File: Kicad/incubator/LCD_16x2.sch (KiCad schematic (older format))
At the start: 6 parts, among them SW2 Rotary_Encoder_Switch

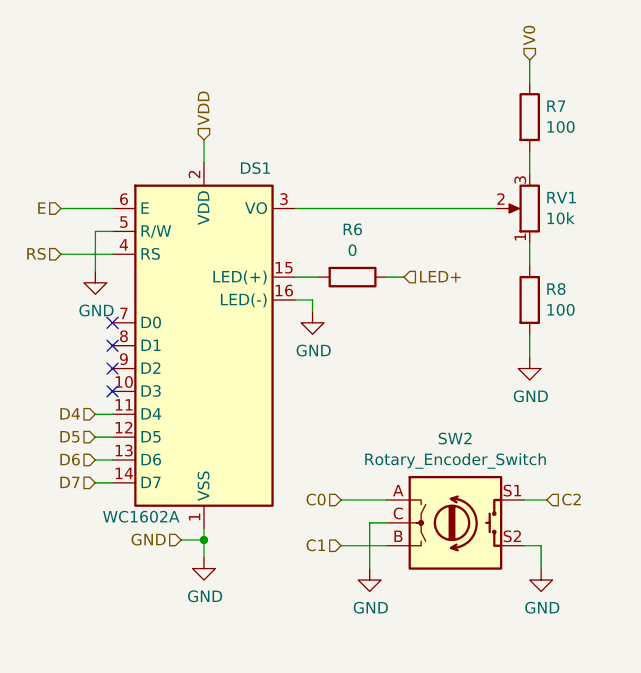
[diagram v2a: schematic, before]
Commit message: fix: iss #1: add ERROR and BLINKING LED, iss #2: solved
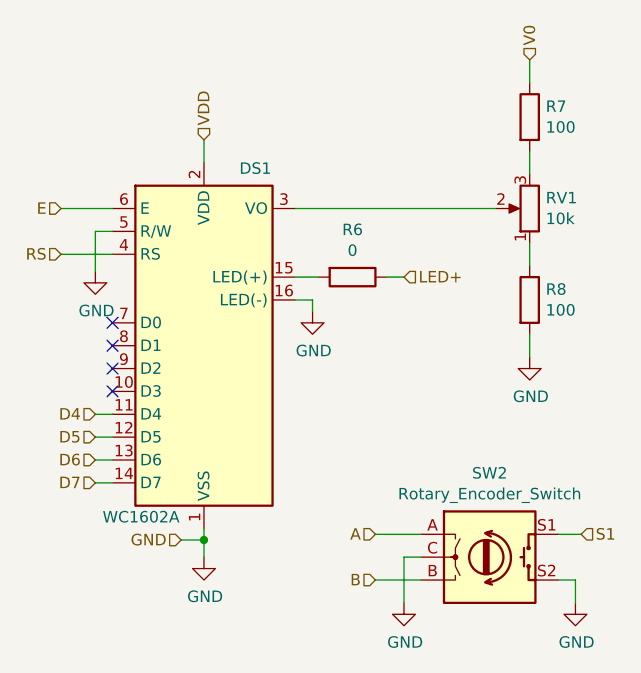
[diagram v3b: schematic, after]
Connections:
- net C0 renamed A
- net C1 renamed B
- net C2 renamed S1
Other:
- moved on the sheet: SW2
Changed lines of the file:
@@
 NoConn ~ 5000 3975
 Wire Wire Line
-	6200 4450 6000 4450
-Wire Wire Line
-	6200 4650 6000 4650
-Wire Wire Line
-	6875 4650 6800 4650
-Wire Wire Line
-	6875 4750 6875 4650
+	6350 4600 6150 4600
+Wire Wire Line
+	6350 4800 6150 4800
+Wire Wire Line
+	7025 4800 6950 4800
+Wire Wire Line
+	7025 4900 7025 4800
 $Comp
 L incubator-rescue:GND-power #PWR?
 U 1 1 611BC109
-P 6875 4750
+P 7025 4900
 AR Path="/611BC109" Ref="#PWR?"  Part="1"
 AR Path="/611AEB1E/611BC109" Ref="#PWR0120"  Part="1"
-F 0 "#PWR0120" H 6875 4500 50  0001 C CNN
-F 1 "GND" H 6880 4577 50  0000 C CNN
-F 2 "" H 6875 4750 50  0001 C CNN
-F 3 "" H 6875 4750 50  0001 C CNN
-	1    6875 4750
-	1    0    0    -1
-$EndComp
-Wire Wire Line
-	6900 4450 6800 4450
-Wire Wire Line
-	6125 4550 6125 4750
-Wire Wire Line
-	6200 4550 6125 4550
+F 0 "#PWR0120" H 7025 4650 50  0001 C CNN
+F 1 "GND" H 7030 4727 50  0000 C CNN
+F 2 "" H 7025 4900 50  0001 C CNN
+F 3 "" H 7025 4900 50  0001 C CNN
+	1    7025 4900
+	1    0    0    -1
+$EndComp
+Wire Wire Line
+	6275 4700 6275 4900
+Wire Wire Line
+	6350 4700 6275 4700
 $Comp
 L incubator-rescue:GND-power #PWR?
 U 1 1 611BC115
-P 6125 4750
+P 6275 4900
 AR Path="/611BC115" Ref="#PWR?"  Part="1"
 AR Path="/611AEB1E/611BC115" Ref="#PWR0121"  Part="1"
-F 0 "#PWR0121" H 6125 4500 50  0001 C CNN
-F 1 "GND" H 6130 4577 50  0000 C CNN
-F 2 "" H 6125 4750 50  0001 C CNN
-F 3 "" H 6125 4750 50  0001 C CNN
-	1    6125 4750
+F 0 "#PWR0121" H 6275 4650 50  0001 C CNN
+F 1 "GND" H 6280 4727 50  0000 C CNN
+F 2 "" H 6275 4900 50  0001 C CNN
+F 3 "" H 6275 4900 50  0001 C CNN
+	1    6275 4900
 	1    0    0    -1
 $EndComp
@@
 L incubator-rescue:Rotary_Encoder_Switch-Device SW?
 U 1 1 611BC160
-P 6500 4550
+P 6650 4700
 AR Path="/611BC160" Ref="SW?"  Part="1"
 AR Path="/611AEB1E/611BC160" Ref="SW2"  Part="1"
-F 0 "SW2" H 6500 4917 50  0000 C CNN
-F 1 "Rotary_Encoder_Switch" H 6500 4826 50  0000 C CNN
-F 2 "Rotary_Encoder:RotaryEncoder_Alps_EC11E-Switch_Vertical_H20mm" H 6350 4710 50  0001 C CNN
-F 3 "~" H 6500 4810 50  0001 C CNN
-	1    6500 4550
+F 0 "SW2" H 6650 5067 50  0000 C CNN
+F 1 "Rotary_Encoder_Switch" H 6650 4976 50  0000 C CNN
+F 2 "Rotary_Encoder:RotaryEncoder_Alps_EC11E-Switch_Vertical_H20mm" H 6500 4860 50  0001 C CNN
+F 3 "~" H 6650 4960 50  0001 C CNN
+	1    6650 4700
 	1    0    0    -1
 $EndComp
@@
 Wire Wire Line
 	5400 4625 5400 4575
-Text HLabel 6000 4450 0    50   Input ~ 0
-C0
-Text HLabel 6000 4650 0    50   Input ~ 0
-C1
-Text HLabel 6900 4450 2    50   Input ~ 0
-C2
+Text HLabel 6150 4800 0    50   Input ~ 0
+B
 Text HLabel 5400 2875 1    50   Input ~ 0
 VDD
@@
 Text HLabel 6825 2525 1    50   Input ~ 0
 V0
+Text HLabel 6150 4600 0    50   Input ~ 0
+A
+Wire Wire Line
+	7050 4600 6950 4600
+Text HLabel 7050 4600 2    50   Input ~ 0
+S1
 $EndSCHEMATC
